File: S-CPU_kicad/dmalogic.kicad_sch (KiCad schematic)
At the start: 86 parts

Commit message: DMA logic update + some mistakes found in gate identification. Found while working out the DMA priority encoder.
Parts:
- removed DNBO: NAND_5, symbol Ricoh_Cells:NAND_5
- added CMYW, DNAW, DNBO, DNBU, DNCN, DNCY, DNDK, EMPN: NAND_2, symbol Ricoh_Cells:NAND_2
- added CNBZ, CNTA, CNUY, DMQT, DMRB, DMSM, DMTA, DNAN, DNCE, EMAU, EMCQ, EMGX (x2), NMTQ: INVERTER_A, symbol Ricoh_Cells:INVERTER_A
- added CNSE, DNAA: NOR_3, symbol Ricoh_Cells:NOR_3
- added DCBP: OR_2, symbol Ricoh_Cells:OR_2
- added DMEC, DMEG, DMEW, EBSG (x7), JMBI, JMBL, JMBL1: DFFR_A, symbol Ricoh_Cells:DFFR_A
- added DMRU, LMFG2, LMFY, MMLQ, MNHE, MNHE2: NOR_2, symbol Ricoh_Cells:NOR_2
- added EMBH, EMES, EMHX: AOI_22, symbol Ricoh_Cells:AOI_22
- added KMCA, KMCA1, KMDK, KMDK1: AND_2, symbol Ricoh_Cells:AND_2
- added PAWC (x5): NOR_LATCH, symbol Ricoh_Cells:NOR_LATCH
- renumbered IMBE1 to KMBX
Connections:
- net EMIZ_IN0 is gone; now on net wDMPK: DMOC.1, DMPK.3
- net +5V: now also EMIZ. (~{OUT7})
- net D5: now also JMBL1.2 (D)
- net D6: now also JMBL.2 (D)
- net D7: now also JMBI.2 (D)
- net ~{420C_WR}: now also GMEX.2, GMNY.2, GMSH.2, GMVF.2, GNBN.2, GNCF.2, GNKJ.2, GNQI.2, JMBI.3 (CLK), JMBI.4 (~{CLK}), JMBL.3 (CLK), JMBL.4 (~{CLK}), JMBL1.3 (CLK), JMBL1.4 (~{CLK})
- net at PAWC.1 (SET): now also PAWC.1 (SET)
- net at KMAZ.1: now also JMBI.6 (Q)
- net at KMAZ.2: now also PAWC.3 (Q)
- net wDNBO: now reaches CNNO.1
- net wDNBO: now also DNAW.1, DNBO.3
- net at FMHZ.6 (Q): now also DNBO.2
- net at LMFG.1: now also EBSG.6 (Q), MNHE.1
- net at LMFG.2: now also LMFY.2
- net at FMKL.6 (Q): now also DNBU.1
- net at FMUY.6 (Q): now also DNBY.1
- net wCMCO: now reaches CMCO.3, CMER.1
- net wCMEU: now reaches CMER.2, CMEU.3, CMKK.1
- net at IMLI.9: now also DNBU.2
- net at EMIZ. (~{OUT7}), GMNG.2: now also EBSG.2 (D)
- net wCNMF_IN1: now reaches EMIZ. (~{OUT7})
- net wCNMF_IN1: now also DMEW.2 (D), EBSG.6 (Q), EMHX.3
- net at EMIZ. (~{OUT7}), GMUF.2: now also EBSG.2 (D)
- net at EMIZ. (~{OUT7}), GMOP.2: now also EBSG.2 (D)
- net wDMPK: now reaches CNRJ.1
- net at CNRJ.3: now also CNSE.2
- net at DNBY.2: now also IMLI.20
- net wDNBY: now reaches CNNO.2, DNBY.3
- net wDNBY: now also DNCN.2, DNDK.2
- net wDMHY: now reaches CMOY.2, DMHY.3, DMOC.2
- net at OBEE.2: now also DCBP.3
- net HDMA_D7: now reaches IMDD.4, KMBK.3
- net HDMA_D6: now reaches IMDD.11
- net HDMA_D6: now also KMDK.3
- net at KMBX.2: now also KMCA.3, KMDK.2
- net at CMTB.2, DMOC.3: now also DNAA.2
- net at CMTB.3: now also CMYW.2
- net at IMLI.7: now also DNBO.1
- net at CNRU.3: now also CNSE.1
- net at IMLI.22: now also EMPN.2
- net HDMA_D5: now reaches IMDD.16
- net HDMA_D5: now also KMDK1.3
- net at FMWM.6 (Q): now also EMPN.1
- net wHMAZ renamed 420B_D7
- net wHMBN renamed 420B_D6
- net wHMDE renamed 420B_D4
- net wHMDM renamed 420B_D3
- net wHMEG renamed 420B_D2
- net wHMFF renamed 420B_D1
- net wHMJO renamed 420B_D0
- net wHMRC renamed 420B_D5
- new net: CMYW.1, DMRB.1, DMRU.3
- new net: CMYW.3, CNBZ.1
- new net: DMEG.1 (~{RESET}), DMEG.5 (~{RESET})
- new net: DMEG.6 (Q), EMES.1
- new net: EBSG.1 (~{RESET}), EBSG.5 (~{RESET}) (x4)
- new net: CNBZ.2, EBSG.2 (D)
- new net: EBSG.3 (CLK), EBSG.3 (CLK), EBSG.3 (CLK), EBSG.3 (CLK), EBSG.4 (~{CLK}), EBSG.4 (~{CLK}), EBSG.4 (~{CLK}), EBSG.4 (~{CLK})
- new net: DMRU.1, DNAN.1, DNAW.3
- new net: DMRU.2, DNAA.3, DNDK.3
- new net: DMSM.2, EBSG.2 (D)
- new net: DNCE.2, DNCN.1
- new net: DNCN.3, DNCY.1
- new net: EMAU.1, EMBH.3
- new net: DMEW.6 (Q), EMHX.1
- new net: EMBH.2, EMES.2, EMGX.2, EMHX.2
- new net: EMGX.1, EMHX.3
- new net: EMBH.4, EMES.4, EMGX.1, EMHX.4
- new net: EBSG.6 (Q), LMFY.1, MMLQ.1
- new net: LMFY.3, PAWC.4 (RESET)
- new net: KMCA.2, PAWC.3 (Q)
- new net: MMLQ.3, PAWC.4 (RESET)
- new net: EMCQ.1, EMES.3
- new net: DMEC.6 (Q), EMBH.1
- new net: EBSG.3 (CLK), EBSG.3 (CLK), EBSG.3 (CLK), EBSG.4 (~{CLK}), EBSG.4 (~{CLK}), EBSG.4 (~{CLK}), NMTQ.2
- new net: KMDK.1, PAWC.3 (Q)
- new net: JMBI.1 (~{RESET}), JMBI.5 (~{RESET}), JMBL.1 (~{RESET}), JMBL.5 (~{RESET}), JMBL1.1 (~{RESET}), JMBL1.5 (~{RESET})
- new net: JMBL1.6 (Q), KMCA1.1
- new net: MNHE.3, PAWC.4 (RESET)
- new net: DMQT.2, EBSG.2 (D)
- new net: DMTA.1, DNAA.4
- new net: DMSM.1, DMTA.2
- new net: EBSG.6 (Q), LMFG2.1, MNHE2.1
- new net: LMFG2.3, PAWC.4 (RESET)
- new net: KMDK1.1, PAWC.3 (Q)
- new net: KMCA1.3, KMDK1.2
- new net: MMLQ.2, MNHE.2
- new net: KMCA1.2, PAWC.3 (Q)
- new net: CNSE.4, CNTA.1
- new net: CNTA.2, CNUY.1
- new net: DNAA.1, DNAN.2
- new net: JMBL.6 (Q), KMCA.1
- new net: CNUY.2, EBSG.2 (D)
- new net: MNHE2.3, PAWC.4 (RESET)
- new net: DMQT.1, DMRB.2
- new net: DMEC.1 (~{RESET}), DMEC.5 (~{RESET})
- new net: CNSE.3, DNCY.3
- new net: DMEW.1 (~{RESET}), DMEW.5 (~{RESET})
- new net DMA_CHAN0: EMGX.2
- new net DMA_CHAN1: EMCQ.2
- new net DMA_CHAN2: EMAU.2
- new net RISING_VBLANK: NMTQ.1, PAWC.1 (SET), PAWC.1 (SET)
- new net wCNDH_DIS: EBSG.6 (Q), EMIZ. (~{OUT7})
- new net wCNFW_IN3: DMEC.2 (D), EBSG.6 (Q), EMBH.3, EMIZ. (~{OUT7})
- new net wCNLW_IN2: DMEG.2 (D), EBSG.6 (Q), EMES.3, EMIZ. (~{OUT7})
- new net wDNBU: DNAW.2, DNBU.3, DNCE.1
- new net wEMPN: DNCY.2, DNDK.1, EMPN.3
- new net wNBEG_wNBEB_XIN/8: DMEC.3 (CLK), DMEC.4 (~{CLK}), DMEG.3 (CLK), DMEG.4 (~{CLK}), DMEW.3 (CLK), DMEW.4 (~{CLK}), EBSG.1 (~{RESET}), EBSG.1 (~{RESET}), EBSG.1 (~{RESET}), EBSG.5 (~{RESET}), EBSG.5 (~{RESET}), EBSG.5 (~{RESET})
- no-connect marks 0 -> 7
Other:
- note added: "DEMUX is disabled when BIT7-0 = "11111111". Priority encoder from bit 7 to bit 0 When BIT7-0 = "0xxxxxxx" => DEMUX input = "111" selecting DMA Channel 7 When BIT7-0 = "10xxxxxx" => DEMUX input = "110" selecting DMA Channel 6 .. When BIT7-0 = "11111110" => DEMUX input = "000" selecting DMA Channel 0"
- moved on the sheet: CMCO, CMER, CMEU, CMKK, CMOY, CMTB, CNNO, CNRJ, DMA?, DMHY, DMOC, DMPK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

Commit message: Further updates in the DMA region. SYS clock identified at last!
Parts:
- added EBSG (x5), JMGD, JMIO, JMIY, JMJE, JMKG: DFFR_A, symbol Ricoh_Cells:DFFR_A
- added KMFF, KMNL, KMVL: OR_3, symbol Ricoh_Cells:OR_3
- added KMGA, KMHD, KMHW, KMLK, KMQC, KMRM, KMSG, KMUQ, KMVO, KMVR: AND_2, symbol Ricoh_Cells:AND_2
- added LMUV, LNHX, LNKU, LNNE, LNTA, MNHM, MNJI, MNNS, MNPG, MOBP, NMSM: NOR_2, symbol Ricoh_Cells:NOR_2
- added MOJA: INVERTER_A, symbol Ricoh_Cells:INVERTER_A
- added PAWC (x10): NOR_LATCH, symbol Ricoh_Cells:NOR_LATCH
- EBSG, EBVQ, EBXE, EBYP, ECCU, ECEK, ECGN, ECGO: value DFFR_A -> DFFR_B; symbol Ricoh_Cells:DFFR_A -> Ricoh_Cells:DFFR_B
- renumbered EMGX to EMIB, JMBL1 to JMCL, KMCA1 to KMEU, KMDK1 to KMEY, LMFG2 to LMPF, MNHE2 to MNOG
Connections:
- net 420B_D0: now also ECGO.7 (Q); no longer ECGO.6 (Q)
- net 420B_D1: now also ECGN.7 (Q); no longer ECGN.6 (Q)
- net 420B_D2: now also ECEK.7 (Q); no longer ECEK.6 (Q)
- net 420B_D3: now also ECCU.7 (Q); no longer ECCU.6 (Q)
- net 420B_D4: now also EBYP.7 (Q); no longer EBYP.6 (Q)
- net 420B_D5: now also EBXE.7 (Q); no longer EBXE.6 (Q)
- net 420B_D6: now also EBVQ.7 (Q); no longer EBVQ.6 (Q)
- net 420B_D7: now also EBSG.7 (Q); no longer EBSG.6 (Q)
- net D0: now also JMKG.2 (D)
- net D1: now also JMJE.2 (D)
- net D2: now also JMIY.2 (D)
- net D3: now also JMIO.2 (D)
- net D4: now also JMGD.2 (D)
- net RISING_VBLANK: now also PAWC.1 (SET), NMSM.1, PAWC.1 (SET), PAWC.1 (SET), PAWC.1 (SET), PAWC.1 (SET), PAWC.1 (SET)
- net wNBEG_wNBEB_XIN/8: now also EBSG.3 (CLK), EBSG.3 (CLK), EBSG.3 (CLK), EBSG.4 (~{CLK}), EBSG.4 (~{CLK}), EBSG.4 (~{CLK}), EBSG.3 (CLK), EBSG.3 (CLK), EBSG.3 (CLK), EBSG.3 (CLK), EBSG.3 (CLK), EBSG.4 (~{CLK}), EBSG.4 (~{CLK}), EBSG.4 (~{CLK}), EBSG.4 (~{CLK}), EBSG.4 (~{CLK}); no longer EBSG.1 (~{RESET}), EBSG.1 (~{RESET}), EBSG.1 (~{RESET}), EBSG.5 (~{RESET}), EBSG.5 (~{RESET}), EBSG.5 (~{RESET})
- net ~{420C_WR}: now also JMGD.3 (CLK), JMGD.4 (~{CLK}), JMIO.3 (CLK), JMIO.4 (~{CLK}), JMIY.3 (CLK), JMIY.4 (~{CLK}), JMJE.3 (CLK), JMJE.4 (~{CLK}), JMKG.3 (CLK), JMKG.4 (~{CLK})
- net at EMIZ. (~{OUT7}), GMYD.2: now also EBSG.2 (D)
- net at PAWC.1 (SET), PAWC.1 (SET): now also PAWC.1 (SET), PAWC.1 (SET), PAWC.1 (SET), PAWC.1 (SET), PAWC.1 (SET), PAWC.1 (SET)
- net 420C_D7: now reaches KMAZ.3, KMBK.2, KMBX.1
- net at LMFG.2, LMFY.2: now also LMPF.1, LMUV.1, LNHX.2, LNKU.1, LNNE.1, LNTA.2, NMSM.3
- net wDCBP_NOHDMA_2: now reaches DCBP.3, OBEE.1
- net at JMBI.1 (~{RESET}), JMBI.5 (~{RESET}), JMBL.1 (~{RESET})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: now also JMGD.1 (~{RESET}), JMGD.5 (~{RESET}), JMIO.1 (~{RESET}), JMIO.5 (~{RESET}), JMIY.1 (~{RESET}), JMIY.5 (~{RESET}), JMJE.1 (~{RESET}), JMJE.5 (~{RESET}), JMKG.1 (~{RESET}), JMKG.5 (~{RESET})
- net at EMIZ. (~{OUT7}), GNSN.2: now also EBSG.2 (D)
- net at LMPF.2: now also EBSG.6 (Q), MNOG.2
- net ~{420C}: now reaches DMA?.1, UBNH.6
- net at EMIZ. (~{OUT7}), GNIX.2: now also EBSG.2 (D)
- net 420C_D5: now reaches KMEU.3, KMEY.2
- net 420C_D5: now also KMFF.1
- net HDMA_D2: now reaches IMLI.11
- net HDMA_D2: now also KMRM.3
- net at EMIZ. (~{OUT7}), GNBU.2: now also EBSG.2 (D)
- net at EMIZ. (~{OUT7}), GNPC.2: now also EBSG.2 (D)
- net at MMLQ.2, MNHE.2: now also MNOG.1, MNHM.2, MNJI.1, MNNS.1, MNPG.1, MOBP.2, MOJA.2
- net 420C_D6: now reaches KMBX.2, KMCA.3, KMDK.2
- net at KMBX.3: now also KMFF.2
- net HDMA_D3: now reaches IMLI.4
- net HDMA_D3: now also KMLK.3
- net HDMA_D4: now reaches IMDD.24
- net HDMA_D4: now also KMHD.3
- net HDMA_D1: now reaches IMLI.16
- net HDMA_D1: now also KMUQ.3
- net HDMA_D0: now reaches IMLI.24
- net HDMA_D0: now also KMVR.3
- net wCMCO renamed DMA_D7
- net wCMEU renamed DMA_D6
- net wDMHY renamed DMA_D5
- net wDMPK renamed DMA_D4
- net wDNBO renamed DMA_D3
- net wDNBU renamed DMA_D2
- net wDNBY renamed DMA_D1
- net wEMPN renamed DMA_D0
- new net: EBSG.6 (Q), LMUV.2, MNPG.2
- new net: MNPG.3, PAWC.4 (RESET)
- new net: EBSG.6 (Q), LNKU.2, MNJI.2
- new net: MNJI.3, PAWC.4 (RESET)
- new net: KMQC.2, PAWC.3 (Q)
- new net: JMGD.6 (Q), KMGA.1
- new net: EBSG.1 (~{RESET}), EBSG.1 (~{RESET}), EBSG.1 (~{RESET}), EBSG.1 (~{RESET}), EBSG.1 (~{RESET}), EBSG.1 (~{RESET}), EBSG.1 (~{RESET}), EBSG.1 (~{RESET}), EBSG.5 (~{RESET}), EBSG.5 (~{RESET}), EBSG.5 (~{RESET}), EBSG.5 (~{RESET}), EBSG.5 (~{RESET}), EBSG.5 (~{RESET}), EBSG.5 (~{RESET}), EBSG.5 (~{RESET}), NMTQ.2
- new net: KMFF.4, KMNL.2
- new net: KMHW.2, PAWC.3 (Q)
- new net: MNHM.3, PAWC.4 (RESET)
- new net: JMIY.6 (Q), KMQC.1
- new net: KMGA.2, PAWC.3 (Q)
- new net: KMHD.1, PAWC.3 (Q)
- new net: LMUV.3, PAWC.4 (RESET)
- new net: KMVR.1, PAWC.3 (Q)
- new net: LNTA.3, PAWC.4 (RESET)
- new net: KMUQ.1, PAWC.3 (Q)
- new net: KMVO.2, PAWC.3 (Q)
- new net: MOBP.3, PAWC.4 (RESET)
- new net: JMKG.6 (Q), KMVO.1
- new net: EBSG.6 (Q), LNHX.1, MNHM.1
- new net: LNHX.3, PAWC.4 (RESET)
- new net: EBSG.6 (Q), LNNE.2, MNNS.2
- new net: LNNE.3, PAWC.4 (RESET)
- new net: KMLK.1, PAWC.3 (Q)
- new net: LNKU.3, PAWC.4 (RESET)
- new net: KMNL.4, KMVL.2
- new net: KMRM.1, PAWC.3 (Q)
- new net: JMJE.6 (Q), KMSG.1
- new net: KMSG.2, PAWC.3 (Q)
- new net: JMIO.6 (Q), KMHW.1
- new net: EBSG.6 (Q), LNTA.1, MOBP.1
- new net: MNNS.3, PAWC.4 (RESET)
- new net 420C_D0: KMVL.3, KMVO.3, KMVR.2
- new net 420C_D1: KMSG.3, KMUQ.2, KMVL.1
- new net 420C_D2: KMNL.3, KMQC.3, KMRM.2
- new net 420C_D3: KMHW.3, KMLK.2, KMNL.1
- new net 420C_D4: KMFF.3, KMGA.3, KMHD.2
- new net ~{NO_HDMA}: KMVL.4
- no-connect marks 7 -> 15
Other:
- note added: "420B WRITE"
- note added: "420C WRITE"
- note added: "8x3 Priority Encoder"
- moved on the sheet: CMCO, CMER, CMEU, CMKK, CMOY, CMTB, CMYW, CNBZ, CNNO, CNRJ, CNRU, CNSE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

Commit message: More updates in DMA section.
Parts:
- removed DCBP: OR_2, symbol Ricoh_Cells:OR_2
- removed OBEE: AND_2, symbol Ricoh_Cells:AND_2
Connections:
- net wSODT: now reaches GMNG.1, GMOP.1, GMUF.1, GMYD.1, GNBU.1, GNIX.1, GNPC.1, GNSN.1
- net wSOGE: now reaches FMCD.1 (~{RESET}), FMCD.5 (~{RESET}), FMFF.1 (~{RESET}), FMFF.5 (~{RESET}), FMGC.1 (~{RESET}), FMGC.5 (~{RESET}), FMHJ.1 (~{RESET}), FMHJ.5 (~{RESET}), FMHZ.1 (~{RESET}), FMHZ.5 (~{RESET}), FMKL.1 (~{RESET}), FMKL.5 (~{RESET}), FMUY.1 (~{RESET}), FMUY.5 (~{RESET}), FMWM.1 (~{RESET}), FMWM.5 (~{RESET})
- net CMYW: now reaches CMYW.3, CNBZ.1
- net wSODM: now reaches EBSG.3 (CLK), EBSG.3 (CLK), EBSG.3 (CLK), EBSG.3 (CLK), EBSG.4 (~{CLK}), EBSG.4 (~{CLK}), EBSG.4 (~{CLK}), EBSG.4 (~{CLK})
- net wDCBP_NOHDMA_2 renamed ~{NO_HDMA2}
- net wNBEG_wNBEB_XIN/8 renamed wNBEB_wNBEG_XIN/8
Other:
- note removed: "from DMA"
- note removed: "to DMA"
- moved on the sheet: CMTB, CMYW, CNBZ, DBWG, DBZJ, DCBP

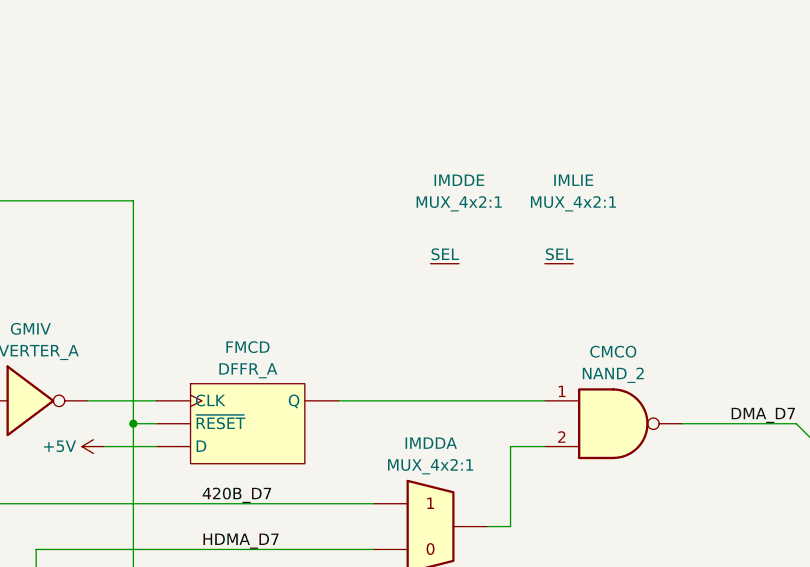
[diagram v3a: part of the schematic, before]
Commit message: Fixed reset signal in DMA section.
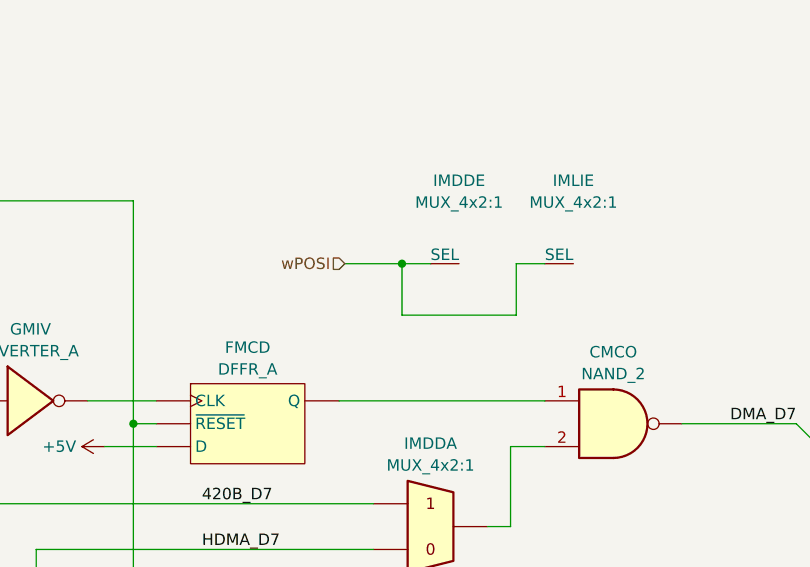
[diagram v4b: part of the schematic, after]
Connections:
- net wPOSI: now reaches IMLI.1 (SEL)
- net wPOSI: now also IMDD.1 (SEL)
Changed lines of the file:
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@@
   (junction (at 95.885 291.465) (diameter 0) (color 0 0 0 0)
   )
+  (junction (at 400.05 57.785) (diameter 0) (color 0 0 0 0)
+  )
   (junction (at 588.645 108.585) (diameter 0) (color 0 0 0 0)
   )
@@
     (stroke (width 0) (type default))
   )
+  (wire (pts (xy 412.75 63.5) (xy 400.05 63.5))
+    (stroke (width 0) (type default))
+  )
   (wire (pts (xy 498.475 389.89) (xy 534.035 389.89))
     (stroke (width 0) (type default))
@@
     (stroke (width 0) (type default))
   )
+  (wire (pts (xy 412.75 57.785) (xy 412.75 63.5))
+    (stroke (width 0) (type default))
+  )
   (wire (pts (xy 205.105 156.21) (xy 220.345 156.21))
     (stroke (width 0) (type default))
@@
     (stroke (width 0) (type default))
   )
+  (wire (pts (xy 400.05 57.785) (xy 403.225 57.785))
+    (stroke (width 0) (type default))
+  )
   (wire (pts (xy 95.885 291.465) (xy 95.885 348.615))
     (stroke (width 0) (type default))
@@
     (stroke (width 0) (type default))
   )
+  (wire (pts (xy 400.05 63.5) (xy 400.05 57.785))
+    (stroke (width 0) (type default))
+  )
   (wire (pts (xy 184.785 400.685) (xy 172.085 400.685))
     (stroke (width 0) (type default))
@@
     (stroke (width 0) (type default))
   )
+  (wire (pts (xy 393.7 57.785) (xy 400.05 57.785))
+    (stroke (width 0) (type default))
+  )
   (wire (pts (xy 179.705 419.735) (xy 184.785 419.735))
     (stroke (width 0) (type default))
@@
     (stroke (width 0) (type default))
   )
+  (wire (pts (xy 415.925 57.785) (xy 412.75 57.785))
+    (stroke (width 0) (type default))
+  )
   (wire (pts (xy 88.265 429.895) (xy 88.265 465.455))
     (stroke (width 0) (type default))
@@
     (effects (font (size 1.27 1.27)) (justify right))
   )
+  (hierarchical_label "wPOSI" (shape input) (at 393.7 57.785 180) (fields_autoplaced)
+    (effects (font (size 1.27 1.27)) (justify right))
+  )

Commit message: Another latch with reset identified. TCKSEL demux cell worked out + notes added to schematics.
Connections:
- net wDBJW_wHASI_RST: now also JMBI.1 (~{RESET}), JMBI.5 (~{RESET}), JMBL.1 (~{RESET}), JMBL.5 (~{RESET}), JMCL.1 (~{RESET}), JMCL.5 (~{RESET}), JMGD.1 (~{RESET}), JMGD.5 (~{RESET}), JMIO.1 (~{RESET}), JMIO.5 (~{RESET}), JMIY.1 (~{RESET}), JMIY.5 (~{RESET}), JMJE.1 (~{RESET}), JMJE.5 (~{RESET}), JMKG.1 (~{RESET}), JMKG.5 (~{RESET})
- net wTOAY: now reaches PAWC.1 (SET), PAWC.1 (SET), PAWC.1 (SET), PAWC.1 (SET), PAWC.1 (SET), PAWC.1 (SET), PAWC.1 (SET), PAWC.1 (SET)
- net CMYW renamed CMYW_EN

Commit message: Almost all cells captured in schematicAlmost all cells captured in schematics. Enter the commit message for your changes. Lines starting
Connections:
- net wXOWO: now reaches EMBH.4, EMES.4, EMHX.4, EMIB.1
- net wWOIX: now reaches NMSM.2
- net wBSEK: now reaches MOJA.1
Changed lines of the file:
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@@
+    (stroke (width 0) (type default))
+  )
+  (wire (pts (xy 35.56 81.28) (xy 58.42 81.28))
     (stroke (width 0) (type default))
   )
@@
     (effects (font (size 1.27 1.27)) (justify right))
   )
+  (hierarchical_label "wXOWO" (shape input) (at 723.9 473.075 180) (fields_autoplaced)
+    (effects (font (size 1.27 1.27)) (justify right))
+  )
   (hierarchical_label "wNBEB_wNBEG_XIN{slash}8" (shape input) (at 74.93 107.95 180) (fields_autoplaced)
     (effects (font (size 1.27 1.27)) (justify right))
@@
     (effects (font (size 1.27 1.27)) (justify left))
   )
+  (hierarchical_label "wWOIX" (shape input) (at 35.56 81.28 180) (fields_autoplaced)
+    (effects (font (size 1.27 1.27)) (justify right))
+  )
+  (hierarchical_label "wBSEK" (shape input) (at 35.56 86.36 180) (fields_autoplaced)
+    (effects (font (size 1.27 1.27)) (justify right))
+  )
   (hierarchical_label "A[0..15]" (shape input) (at 495.3 86.995 180) (fields_autoplaced)

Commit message: Progress in DMA section. Fixed some DFF output issues.
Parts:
- FMCD, FMFF, FMGC, FMHJ, FMHZ, FMKL, FMUY, FMWM: value DFFR_A -> DFFR_B; symbol Ricoh_Cells:DFFR_A -> Ricoh_Cells:DFFR_B
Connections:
- net wDBJW_wHASI_RST: now also GMEX.2, GMNY.2, GMSH.2, GMVF.2, GNBN.2, GNCF.2, GNKJ.2, GNQI.2
- net ~{420C_WR}: no longer GMEX.2, GMNY.2, GMSH.2, GMVF.2, GNBN.2, GNCF.2, GNKJ.2, GNQI.2
- net wSODM renamed NEXT_CHAN_CLK
- net wSODT renamed ~{GDMA_CHAN_RST}
- net wSOGE renamed ~{STOP_DMA}
- no-connect marks 15 -> 23
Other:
- moved on the sheet: GMIV, GMOL, GMTW, GMXT, GNBQ, GNIU, GNOJ, GNSB

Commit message: Update in DMA sections - most debug signals identified. Error found in SYS clk generation. Simulation show correct 6, 8 and 12 cycle SYSCLK modes.
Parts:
- added CMVK, CMVW: INVERTER_A, symbol Ricoh_Cells:INVERTER_A
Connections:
- net 420B_D0: now also IMLI.24; no longer IMLI.25
- net 420B_D1: now also IMLI.16; no longer IMLI.15
- net 420B_D2: now also IMLI.11; no longer IMLI.13
- net 420B_D3: now also IMLI.4; no longer IMLI.5
- net 420B_D4: now also IMDD.24; no longer IMDD.25
- net 420B_D5: now also IMDD.16; no longer IMDD.15
- net 420B_D6: now also IMDD.11; no longer IMDD.13
- net 420B_D7: now also IMDD.4; no longer IMDD.5
- net HDMA_D0: now also IMLI.25; no longer IMLI.24
- net HDMA_D1: now also IMLI.15; no longer IMLI.16
- net HDMA_D2: now also IMLI.13; no longer IMLI.11
- net HDMA_D3: now also IMLI.5; no longer IMLI.4
- net HDMA_D4: now also IMDD.25; no longer IMDD.24
- net HDMA_D5: now also IMDD.15; no longer IMDD.16
- net HDMA_D6: now also IMDD.13; no longer IMDD.11
- net HDMA_D7: now also IMDD.5; no longer IMDD.4
- net at PAWC.3 (Q): now also KMHW.1; no longer KMHW.2
- net at JMIO.6 (Q): now also KMHW.2; no longer KMHW.1
- net CMYW_EN: no longer names the net of CMYW.3, CNBZ.1
- net CMYW_EN: now also CMVW.1
- net RISING_VBLANK renamed FALLING_VBLANK
- net wBSEK renamed HDMA_CHAN_RST
- net wCNDH_DIS renamed wCNDH_~{EN}
- net wPOSI renamed HDMA_TRANSFER
- net wTOAY renamed ENABLE_HDMA_CHANNELS
- net wWOIX renamed DISABLE_HDMA_CHANNEL
- net ~{NO_DMA} renamed GDMA
- net ~{NO_HDMA2} renamed HDMA_EN
- net ~{NO_HDMA} renamed HDMA
- net ~{STOP_DMA} renamed ~{RESTART_DMA}
- new net: CMVK.1, CMVW.2
- new net DMA_TO_BE_SERVICED: CMVK.2
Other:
- note added: "Active low signals"
- moved on the sheet: IMDDE, IMLIE
